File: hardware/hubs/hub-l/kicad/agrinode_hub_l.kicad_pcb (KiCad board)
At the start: 2 copper layers, 130 x 96 mm, 105 parts, among them J1 DC 12V 5.5/2.1, J2 DC IN 7-24V, J3 SOLAR 6-24V, J4 USB 5V / PROG, J5 BAT NTC 10k, J6 PROG, J7 I2C, J8 LED STRIP WS2813, J9 RS-485, Q1 AO3401A, Q2 AO3401A, Q3 MMBT3904, Q4 MMBT3904, Q5 BSS138, Q6 MMBT3904, SW1 RESET, SW2 BOOT / PAIR, U1 LM2596S-5.0, U2 TP4056, U3 MIC29302WU, U4 ESP32-WROOM-32E-N8, U5 CH340C, U6 DS3231MZ, U7 MAX3485ESA, U8 Ra-02 SX1278 433MHz

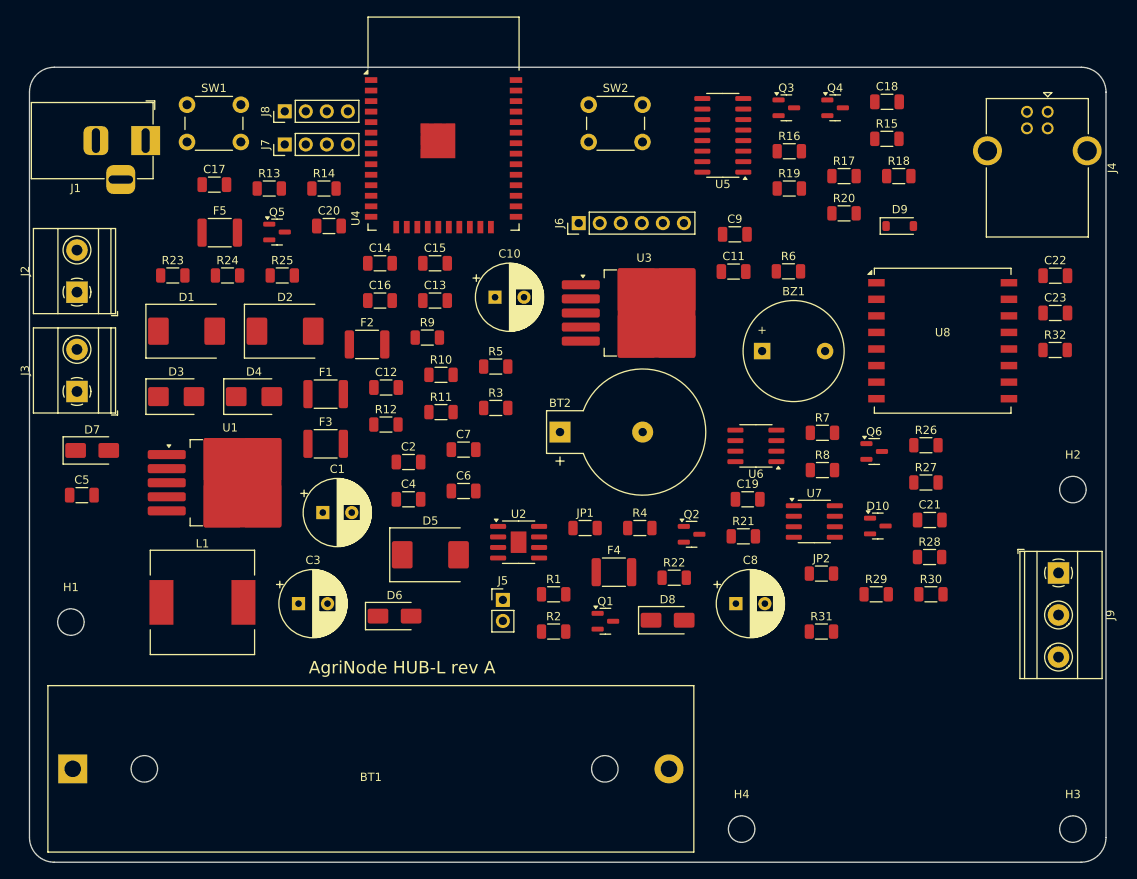
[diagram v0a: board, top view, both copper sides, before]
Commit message: HUB-L: routed, one 11 mm wire jumper (W1, auto-reset base), 0 clearance errors; renders and Gerbers
Co-Authored-By: Claude Opus 5.5 <noreply@anthropic.com>
Claude-Session: https://claude.ai/code/session_014J7amXZ5Y6AZWEh5CjDNja
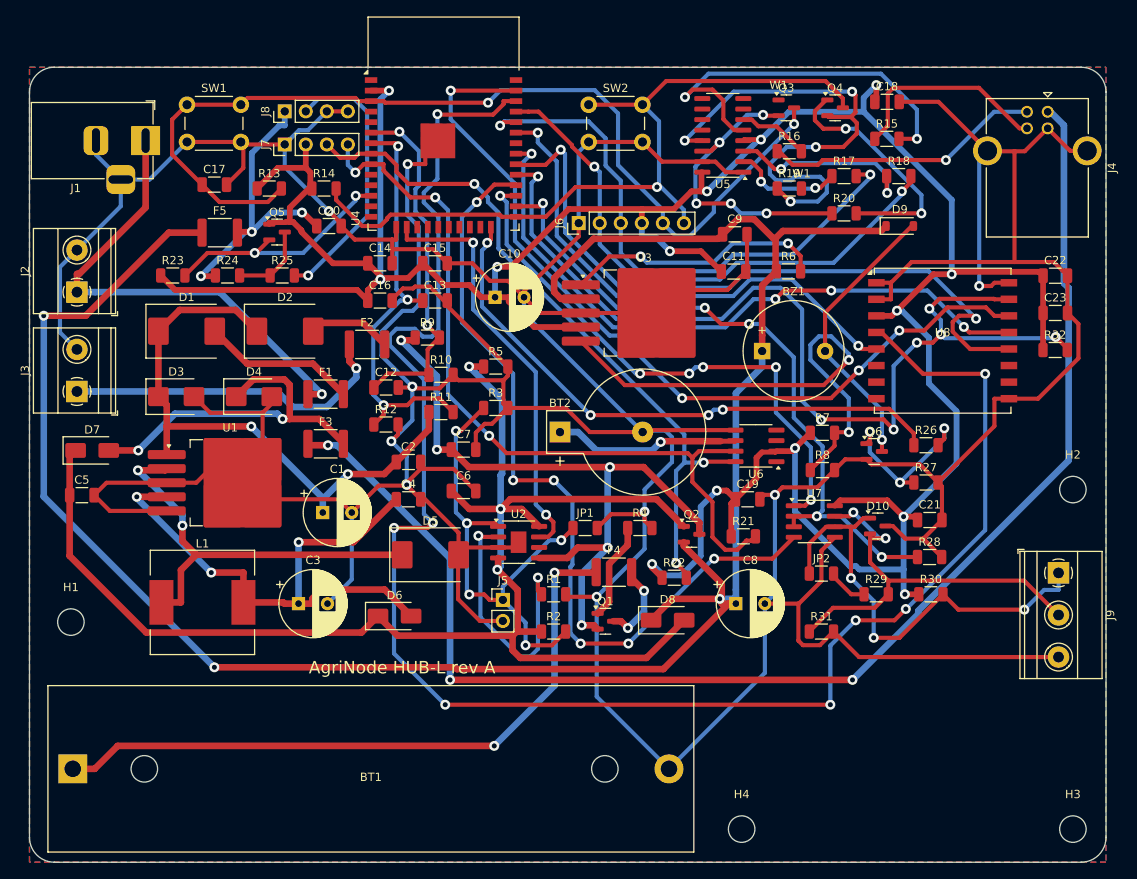
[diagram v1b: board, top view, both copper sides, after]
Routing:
- net GND: track 0.00 -> 811.4 mm, vias 0 -> 9
- net +3V3: track 0.00 -> 371.1 mm, vias 0 -> 14
- net VSYS: track 0.00 -> 258.2 mm, vias 0 -> 3
- net LORA_RST: track 0.00 -> 210.7 mm, vias 0 -> 8
- net /Power - 12V, solar and USB inputs, 18650 charger, rails/V5: track 0.00 -> 175.1 mm, vias 0 -> 3
- net /Power - 12V, solar and USB inputs, 18650 charger, rails/VUSB_RAW: track 0.00 -> 166.8 mm, vias 0 -> 3
- net LORA_CS: track 0.00 -> 118.2 mm, vias 0 -> 7
- net /ESP32, programming, buttons, RTC, LED strip, buzzer/ESP_EN: track 0.00 -> 117.6 mm, vias 0 -> 2
- net SPI_MOSI: track 0.00 -> 101.7 mm, vias 0 -> 4
- net RS485_TX: track 0.00 -> 99.8 mm, vias 0 -> 6
- net /ESP32, programming, buttons, RTC, LED strip, buzzer/I2C_SDA: track 0.00 -> 95.7 mm, vias 0 -> 3
- net /ESP32, programming, buttons, RTC, LED strip, buzzer/BOOT_BTN: track 0.00 -> 94.3 mm, vias 0 -> 1
- net /ESP32, programming, buttons, RTC, LED strip, buzzer/I2C_SCL: track 0.00 -> 85.9 mm, vias 0 -> 3
- net /Power - 12V, solar and USB inputs, 18650 charger, rails/VBAT: track 0.00 -> 85.0 mm, vias 0 -> 5
- net SPI_SCK: track 0.00 -> 84.1 mm, vias 0 -> 2
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- added copper zone on B.Cu, net GND
- added copper zone on F.Cu, net GND
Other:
- board text added: "W1"

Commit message: hubs: routing progress snapshot (HUB-L finished version is 390263c)
Co-Authored-By: Claude Opus 5.5 <noreply@anthropic.com>
Claude-Session: https://claude.ai/code/session_014J7amXZ5Y6AZWEh5CjDNja
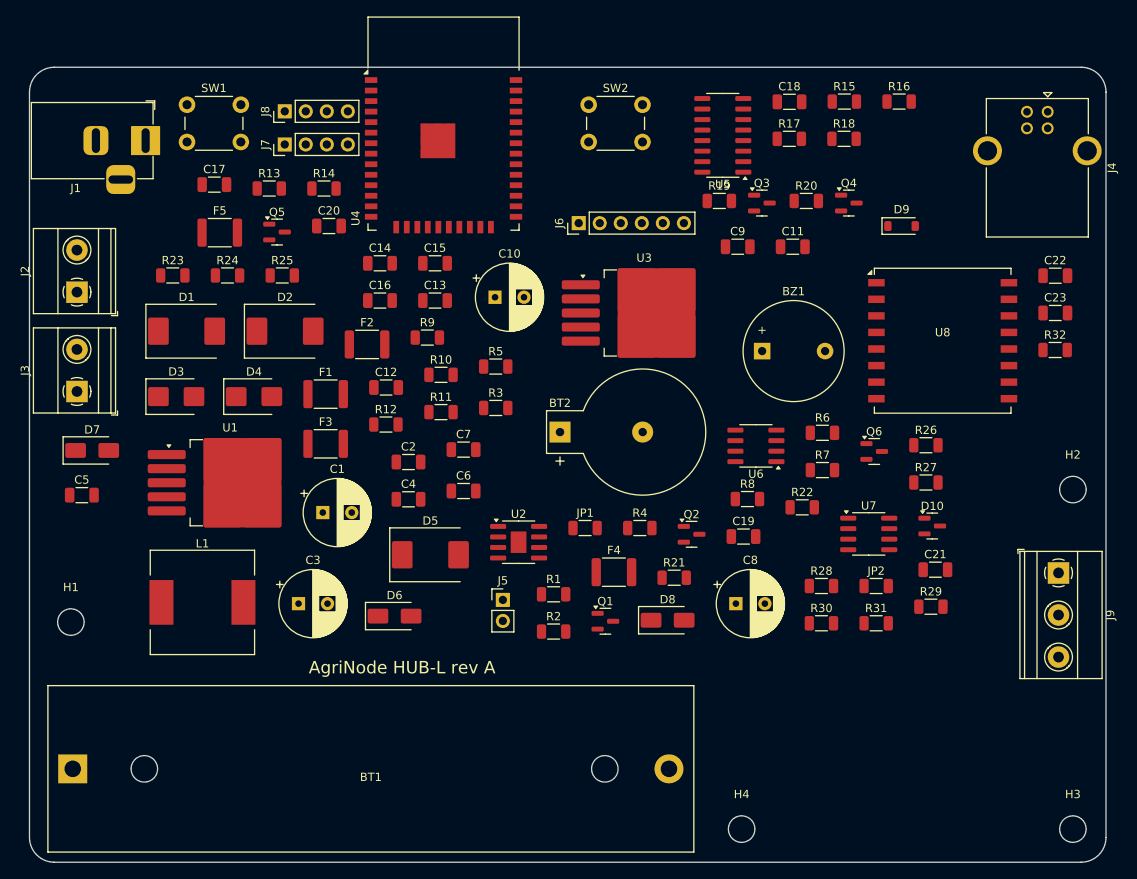
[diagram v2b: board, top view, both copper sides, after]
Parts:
- moved R6 19.9 mm to (145.8, 94.1)
- moved R22 17.6 mm to (143.3, 103.1)
- moved R16 14.6 mm to (155.0, 54.1)
- moved R30 13.7 mm to (145.6, 117.1)
- moved R28 13.5 mm to (145.6, 112.6)
- moved Q3 11.9 mm to (138.4, 66.4)
- moved C18 11.8 mm to (141.8, 54.2)
- moved Q4 11.6 mm to (148.9, 66.4)
- moved R21 9.73 mm to (127.9, 111.6)
- moved R8 9.70 mm to (136.7, 102.1)
- moved R19 8.58 mm to (133.3, 66.1)
- moved R17 8.00 mm to (141.8, 58.6)
- moved R18 8.00 mm to (148.4, 58.6)
- moved C11 7.75 mm to (142.2, 71.7)
- moved R15 6.82 mm to (148.4, 54.1)
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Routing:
- net GND: track 811.4 -> 0.00 mm, vias 9 -> 0
- net +3V3: track 371.1 -> 0.00 mm, vias 14 -> 0
- net VSYS: track 258.2 -> 0.00 mm, vias 3 -> 0
- net LORA_RST: track 210.7 -> 0.00 mm, vias 8 -> 0
- net /Power - 12V, solar and USB inputs, 18650 charger, rails/V5: track 175.1 -> 0.00 mm, vias 3 -> 0
- net /Power - 12V, solar and USB inputs, 18650 charger, rails/VUSB_RAW: track 166.8 -> 0.00 mm, vias 3 -> 0
- net LORA_CS: track 118.2 -> 0.00 mm, vias 7 -> 0
- net /ESP32, programming, buttons, RTC, LED strip, buzzer/ESP_EN: track 117.6 -> 0.00 mm, vias 2 -> 0
- net SPI_MOSI: track 101.7 -> 0.00 mm, vias 4 -> 0
- net RS485_TX: track 99.8 -> 0.00 mm, vias 6 -> 0
- net /ESP32, programming, buttons, RTC, LED strip, buzzer/I2C_SDA: track 95.7 -> 0.00 mm, vias 3 -> 0
- net /ESP32, programming, buttons, RTC, LED strip, buzzer/BOOT_BTN: track 94.3 -> 0.00 mm, vias 1 -> 0
- net /ESP32, programming, buttons, RTC, LED strip, buzzer/I2C_SCL: track 85.9 -> 0.00 mm, vias 3 -> 0
- net /Power - 12V, solar and USB inputs, 18650 charger, rails/VBAT: track 85.0 -> 0.00 mm, vias 5 -> 0
- net SPI_SCK: track 84.1 -> 0.00 mm, vias 2 -> 0
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- removed copper zone on B.Cu, net GND
- removed copper zone on F.Cu, net GND
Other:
- board text removed: "W1"

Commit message: hubs: HUB-L back on its routed layout (1 jumper); auto-reset pinning only for HUB-C and GW-LAN
Co-Authored-By: Claude Opus 5.5 <noreply@anthropic.com>
Claude-Session: https://claude.ai/code/session_014J7amXZ5Y6AZWEh5CjDNja
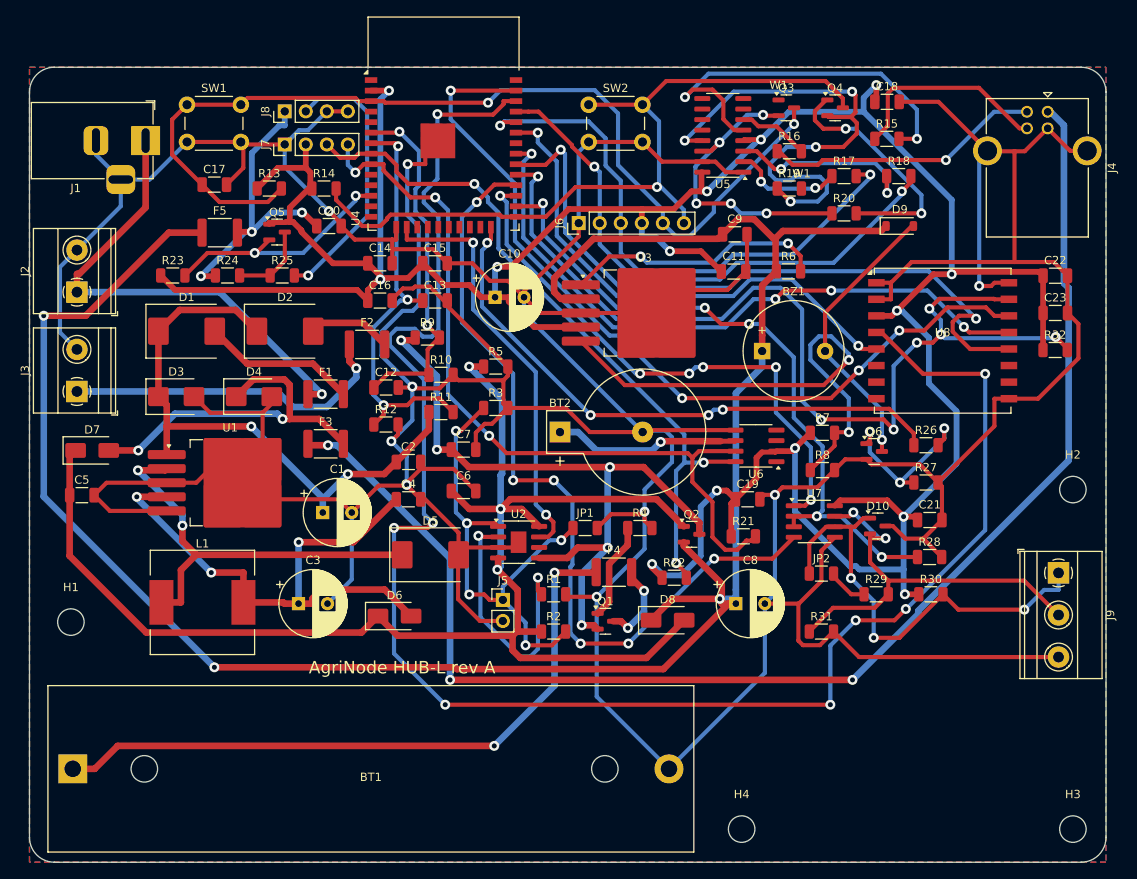
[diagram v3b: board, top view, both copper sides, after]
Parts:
- moved R6 19.9 mm to (141.7, 74.6)
- moved R22 17.6 mm to (127.9, 111.6)
- moved R16 14.6 mm to (141.8, 60.1)
- moved R30 13.7 mm to (158.9, 113.6)
- moved R28 13.5 mm to (158.7, 109.1)
- moved Q3 11.9 mm to (141.4, 54.9)
- moved C18 11.8 mm to (153.6, 54.2)
- moved Q4 11.6 mm to (147.3, 54.9)
- moved R21 9.73 mm to (136.2, 106.6)
- moved R8 9.70 mm to (145.8, 98.6)
- moved R19 8.58 mm to (141.8, 64.6)
- moved R17 8.00 mm to (148.4, 63.1)
- moved R18 8.00 mm to (155.0, 63.1)
- moved C11 7.75 mm to (135.0, 74.7)
- moved R15 6.82 mm to (153.5, 58.6)
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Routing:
- net GND: track 0.00 -> 811.4 mm, vias 0 -> 9
- net +3V3: track 0.00 -> 371.1 mm, vias 0 -> 14
- net VSYS: track 0.00 -> 258.2 mm, vias 0 -> 3
- net LORA_RST: track 0.00 -> 210.7 mm, vias 0 -> 8
- net /Power - 12V, solar and USB inputs, 18650 charger, rails/V5: track 0.00 -> 175.1 mm, vias 0 -> 3
- net /Power - 12V, solar and USB inputs, 18650 charger, rails/VUSB_RAW: track 0.00 -> 166.8 mm, vias 0 -> 3
- net LORA_CS: track 0.00 -> 118.2 mm, vias 0 -> 7
- net /ESP32, programming, buttons, RTC, LED strip, buzzer/ESP_EN: track 0.00 -> 117.6 mm, vias 0 -> 2
- net SPI_MOSI: track 0.00 -> 101.7 mm, vias 0 -> 4
- net RS485_TX: track 0.00 -> 99.8 mm, vias 0 -> 6
- net /ESP32, programming, buttons, RTC, LED strip, buzzer/I2C_SDA: track 0.00 -> 95.7 mm, vias 0 -> 3
- net /ESP32, programming, buttons, RTC, LED strip, buzzer/BOOT_BTN: track 0.00 -> 94.3 mm, vias 0 -> 1
- net /ESP32, programming, buttons, RTC, LED strip, buzzer/I2C_SCL: track 0.00 -> 85.9 mm, vias 0 -> 3
- net /Power - 12V, solar and USB inputs, 18650 charger, rails/VBAT: track 0.00 -> 85.0 mm, vias 0 -> 5
- net SPI_SCK: track 0.00 -> 84.1 mm, vias 0 -> 2
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- added copper zone on B.Cu, net GND
- added copper zone on F.Cu, net GND
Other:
- board text added: "W1"
